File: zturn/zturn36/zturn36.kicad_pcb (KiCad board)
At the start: 4 copper layers, 189.9 x 136.5 mm, 62 parts, among them J11 Conn_02x40_Odd_Even, J12 Conn_02x40_Odd_Even, J5V1 Conn_01x03, Q1 SSM6N15AFU, Q2 SSM6N15AFU, Q3 SSM6N15AFU, Q4 SSM6N15AFU, Q5 SSM6N15AFU, Q6 SSM6N15AFU, Q7 SSM6N15AFU, Q8 SSM6N15AFU, Q9 SSM6N15AFU, U1 74AXP4T245, U10 74AXP4T245, U11 74AXP4T245, U12 74AXP4T245, U13 74AXP4T245, U2 74AXP4T245, U3 74AXP4T245, U8 74AXP4T245, U9 74AXP4T245

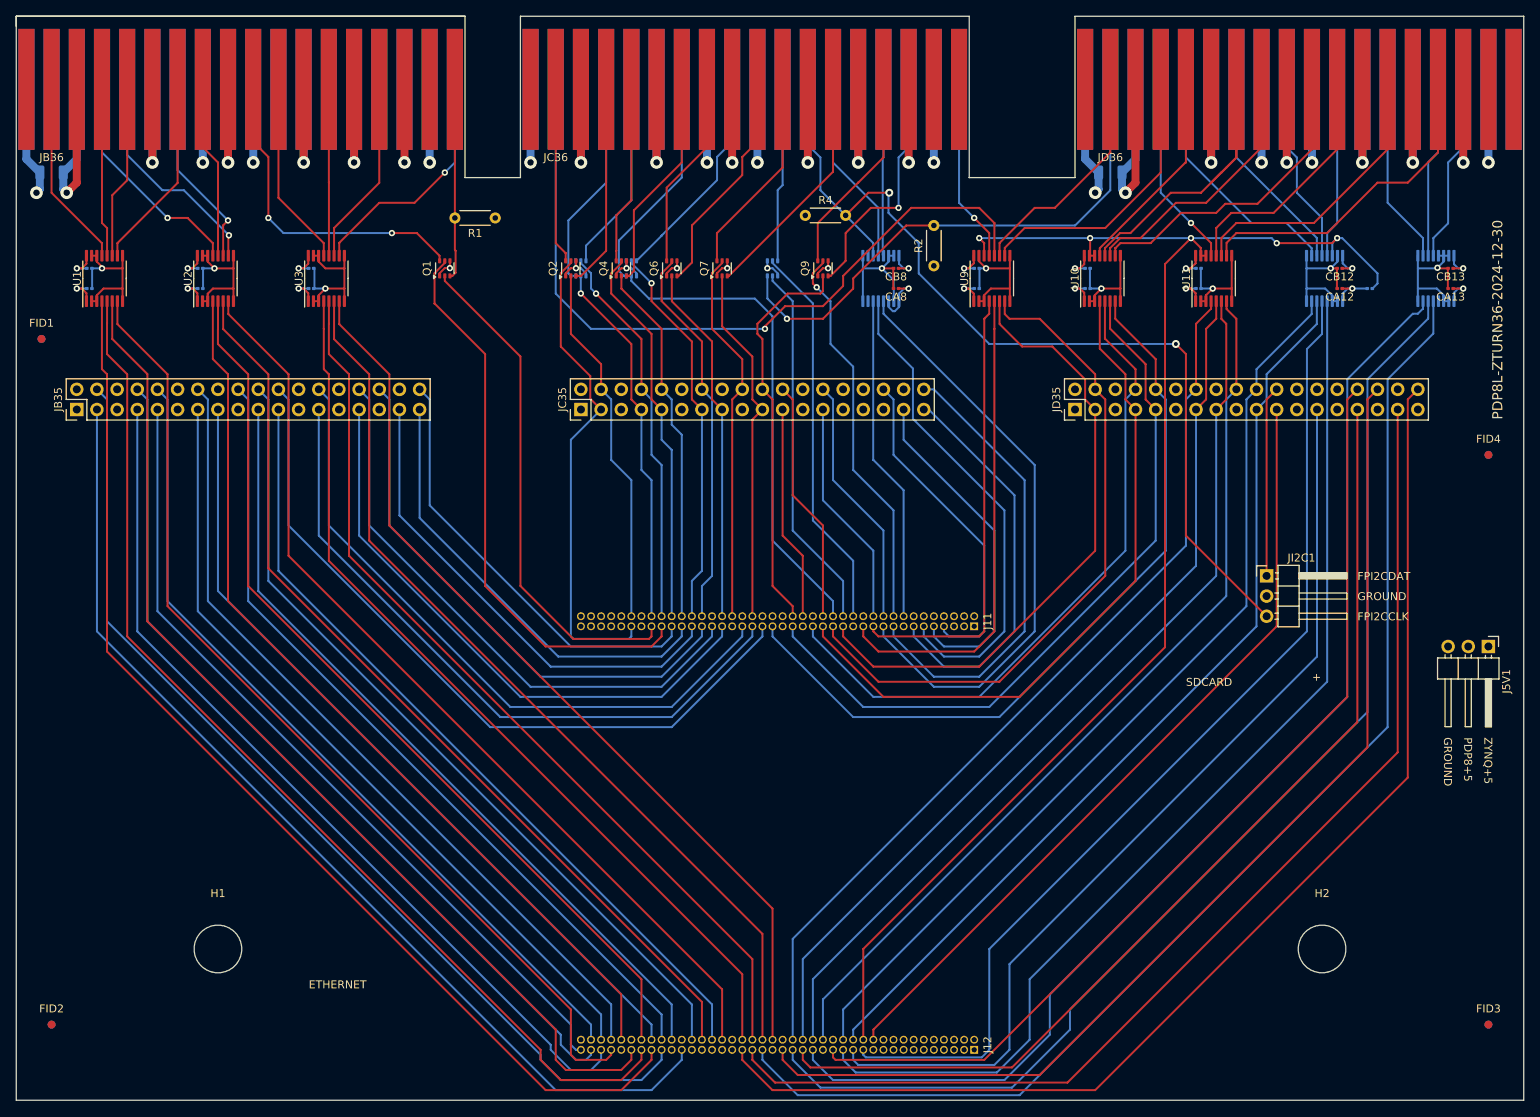
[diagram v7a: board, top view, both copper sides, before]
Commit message: update zturn36,35 pcbs to put i2c at 3.3V and open-collector
...directly from FPGA pins with 2.2K pullups
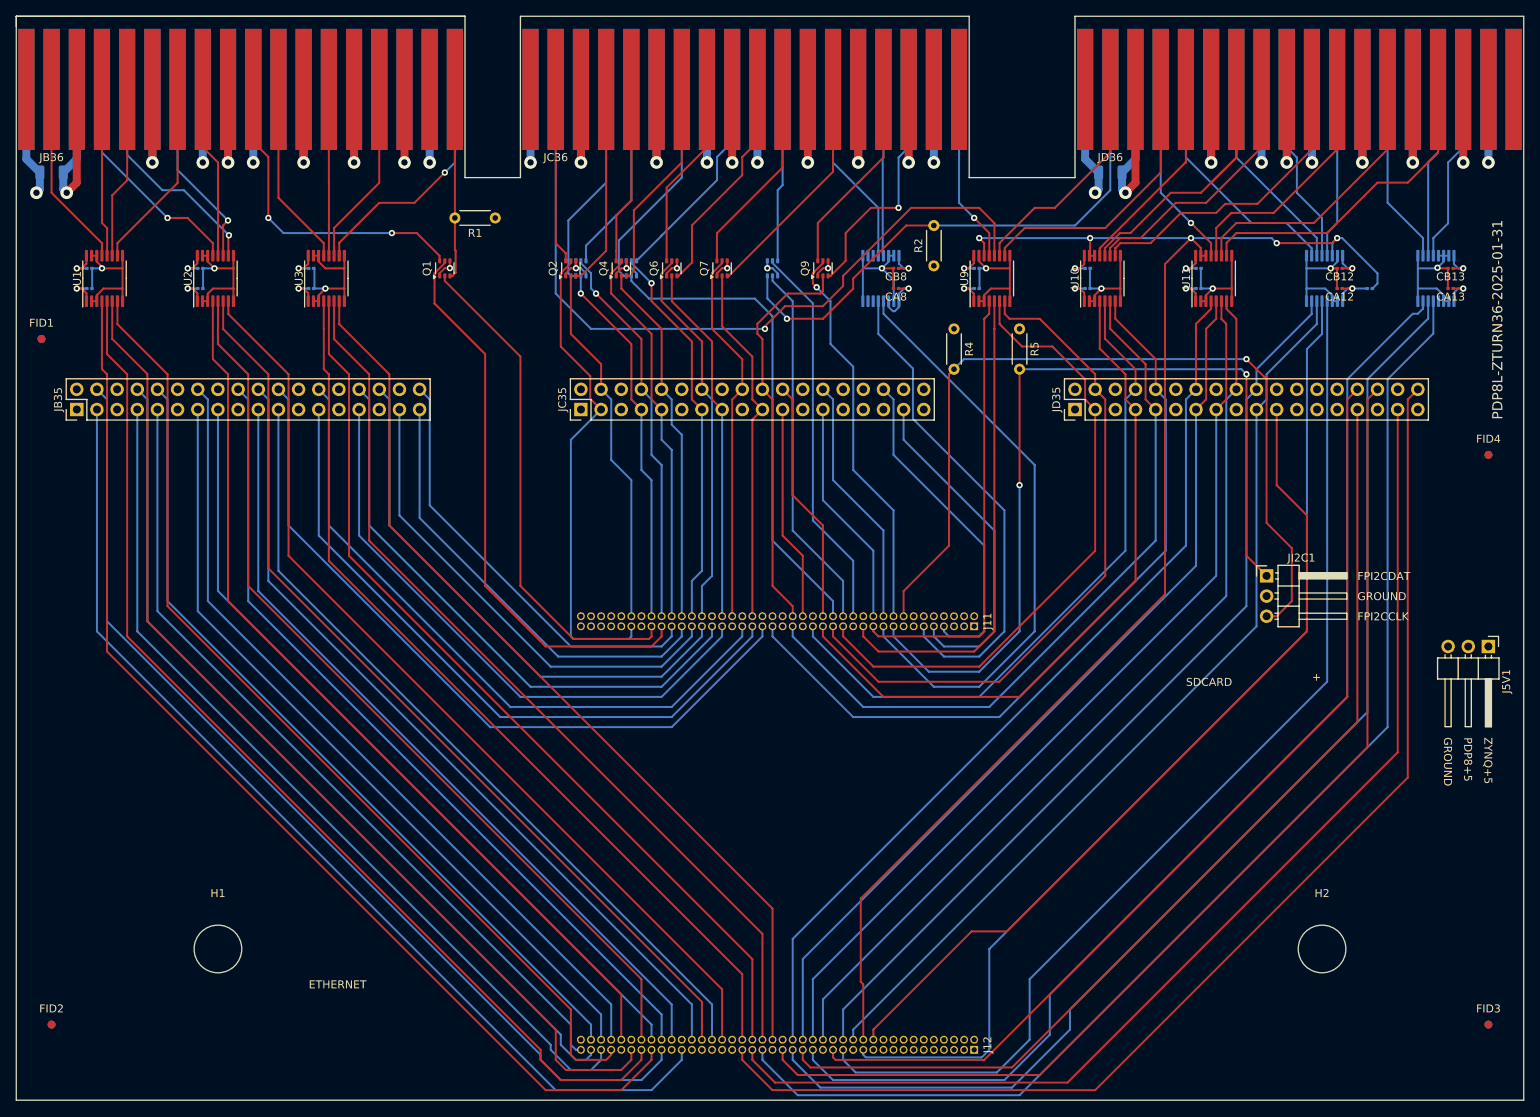
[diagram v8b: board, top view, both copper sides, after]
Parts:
- added R5: 2.2K, Resistor_THT:R_Axial_DIN0204_L3.6mm_D1.6mm_P5.08mm_Horizontal, F.Cu at (126.4, 39.4)
- R4: value 1K -> 2.2K
- moved R4 23.6 mm to (118.1, 39.4), turned to -90 degrees
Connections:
- J11 pad 13: /FPI2CDDIR -> unconnected-(J11-Pin_13-Pad13)
- J11 pad 17: /FPI2CDATA -> /FPI2CDAT
- J12 pad 25: /FPI2CDENA -> unconnected-(J12-Pin_25-Pad25)
- JC35 pad 35: /FPI2CDDIR -> unconnected-(JC35-Pin_35-Pad35)
- JC35 pad 36: /FPI2CDATA -> unconnected-(JC35-Pin_36-Pad36)
- JC36 pad N2: /EPI2CCLK -> unconnected-(JC36-PadN2)
- JD35 pad 22: /EPI2CDAT -> unconnected-(JD35-Pin_22-Pad22)
- JD35 pad 25: /FPI2CDENA -> unconnected-(JD35-Pin_25-Pad25)
- JI2C1 pad 1: /EPI2CDAT -> /FPI2CDAT
- JI2C1 pad 3: /EPI2CCLK -> /FPI2CCLK
- R4 pad 1: +5V -> +3V3
- R4 pad 2: /EPI2CCLK -> /FPI2CCLK
- U8 pad 11: /EPI2CCLK -> unconnected-(U8-2B1-Pad11)
- U8 pad 6: /FPI2CCLK -> unconnected-(U8-2A1-Pad6)
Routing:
- net /FPI2CDENA: track 118.7 -> 0.00 mm
- net /EPI2CCLK: track 110.9 -> 0.00 mm, vias 2 -> 0
- net /FPI2CDAT: track 0.00 -> 108.8 mm, vias 0 -> 2
- net /FPI2CCLK: track 41.3 -> 108.1 mm, vias 0 -> 1
- net /FPI2CDATA: track 58.7 -> 0.00 mm
- net /FPI2CDDIR: track 49.8 -> 0.00 mm
- net /EPI2CDAT: track 24.0 -> 0.00 mm
- net /x_INPUTBUS: track 100.4 -> 106.2 mm
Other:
- board text added: "PDP8L-ZTURN36-2025-01-31"
- board text removed: "PDP8L-ZTURN36-2024-12-30"
